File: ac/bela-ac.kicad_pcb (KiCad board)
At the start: 2 copper layers, 29 parts, among them P5 +/-15v, P6 15v_out, P7 belaaudioout, P8 belaaudioin, P9 mod_ac-io, U1 TL074

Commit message: consolidated schematics etc
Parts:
- removed R4: bead, xnorman:Resistor_Vertical_RM5mm-xnor
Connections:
- P6 pad 1: Net-(P6-Pad1) -> +15v

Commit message: removed ac from extra, added power connection for 15
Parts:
- P6: footprint Pin_Headers:Pin_Header_Straight_1x02_Pitch2.54mm -> mta-156:MTA-156-2
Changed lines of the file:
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@@
     )
   )
-  (module Pin_Headers:Pin_Header_Straight_1x02_Pitch2.54mm (layer F.Cu)
+  (module mta-156:MTA-156-2 (layer F.Cu)
     (at 95.7072 118.618 270)
-    (descr "Through hole straight pin header, 1x02, 2.54mm pitch, single row")
-    (tags "Through hole pin header THT 1x02 2.54mm single row")
-    (fp_text reference P6 (at 0 -2.39 270) (layer F.SilkS)
+    (descr MTA-156-2)
+    (tags MTA-156-2)
+    (fp_text reference P6 (at 0 -5.1 270) (layer F.SilkS)
       (effects (font (size 1 1) (thickness 0.15)))
     )
-    (fp_text value 15v_out (at 0 4.93 270) (layer F.Fab)
+    (fp_text value 15v_out (at 0 -3.1 270) (layer F.Fab)
       (effects (font (size 1 1) (thickness 0.15)))
     )
-    (fp_line (start -1.27 -1.27) (end -1.27 3.81) (layer F.Fab) (width 0.1))
-    (fp_line (start -1.27 3.81) (end 1.27 3.81) (layer F.Fab) (width 0.1))
-    (fp_line (start 1.27 3.81) (end 1.27 -1.27) (layer F.Fab) (width 0.1))
-    (fp_line (start 1.27 -1.27) (end -1.27 -1.27) (layer F.Fab) (width 0.1))
-    (fp_line (start -1.39 1.27) (end -1.39 3.93) (layer F.SilkS) (width 0.12))
-    (fp_line (start -1.39 3.93) (end 1.39 3.93) (layer F.SilkS) (width 0.12))
-    (fp_line (start 1.39 3.93) (end 1.39 1.27) (layer F.SilkS) (width 0.12))
-    (fp_line (start 1.39 1.27) (end -1.39 1.27) (layer F.SilkS) (width 0.12))
-    (fp_line (start -1.39 0) (end -1.39 -1.39) (layer F.SilkS) (width 0.12))
-    (fp_line (start -1.39 -1.39) (end 0 -1.39) (layer F.SilkS) (width 0.12))
-    (fp_line (start -1.6 -1.6) (end -1.6 4.1) (layer F.CrtYd) (width 0.05))
-    (fp_line (start -1.6 4.1) (end 1.6 4.1) (layer F.CrtYd) (width 0.05))
-    (fp_line (start 1.6 4.1) (end 1.6 -1.6) (layer F.CrtYd) (width 0.05))
-    (fp_line (start 1.6 -1.6) (end -1.6 -1.6) (layer F.CrtYd) (width 0.05))
-    (pad 1 thru_hole rect (at 0 0 270) (size 1.7 1.7) (drill 1) (layers *.Cu *.Mask)
+    (fp_line (start 3 -1.6) (end 3 5.6) (layer F.SilkS) (width 0.15))
+    (fp_line (start -4 -1.6) (end -4 5.6) (layer F.SilkS) (width 0.15))
+    (fp_line (start -2.6 -1.6) (end -2.6 5.6) (layer F.SilkS) (width 0.15))
+    (fp_line (start 3.2 -1.8) (end 3.2 5.8) (layer F.CrtYd) (width 0.15))
+    (fp_line (start -4.2 -1.8) (end -4.2 5.8) (layer F.CrtYd) (width 0.15))
+    (fp_line (start -4.2 -1.6) (end -2.6 -1.6) (layer F.SilkS) (width 0.15))
+    (fp_line (start -4.2 -1.6) (end 3 -1.6) (layer F.SilkS) (width 0.15))
+    (fp_line (start 3 5.6) (end -4 5.6) (layer F.SilkS) (width 0.15))
+    (fp_line (start 3.2 -1.8) (end -4.2 -1.8) (layer F.CrtYd) (width 0.15))
+    (fp_line (start -4.2 5.8) (end 3.2 5.8) (layer F.CrtYd) (width 0.15))
+    (pad 1 thru_hole oval (at 0 0 270) (size 5 2.5) (drill 1.68) (layers *.Cu *.Mask F.SilkS)
       (net 22 +15v))
-    (pad 2 thru_hole oval (at 0 2.54 270) (size 1.7 1.7) (drill 1) (layers *.Cu *.Mask)
+    (pad 2 thru_hole oval (at 0 3.96 270) (size 5 2.5) (drill 1.68) (layers *.Cu *.Mask F.SilkS)
       (net 1 GND))
-    (model Pin_Headers.3dshapes/Pin_Header_Straight_1x02_Pitch2.54mm.wrl
-      (at (xyz 0 -0.05 0))
-      (scale (xyz 1 1 1))
-      (rotate (xyz 0 0 90))
-    )
   )
   (gr_text "MOVE AC TO ANOTHER PCB AND PUT 15V in on this board?\n\nAdd mounting holes to AC board" (at 52.1716 109.1184) (layer F.SilkS)

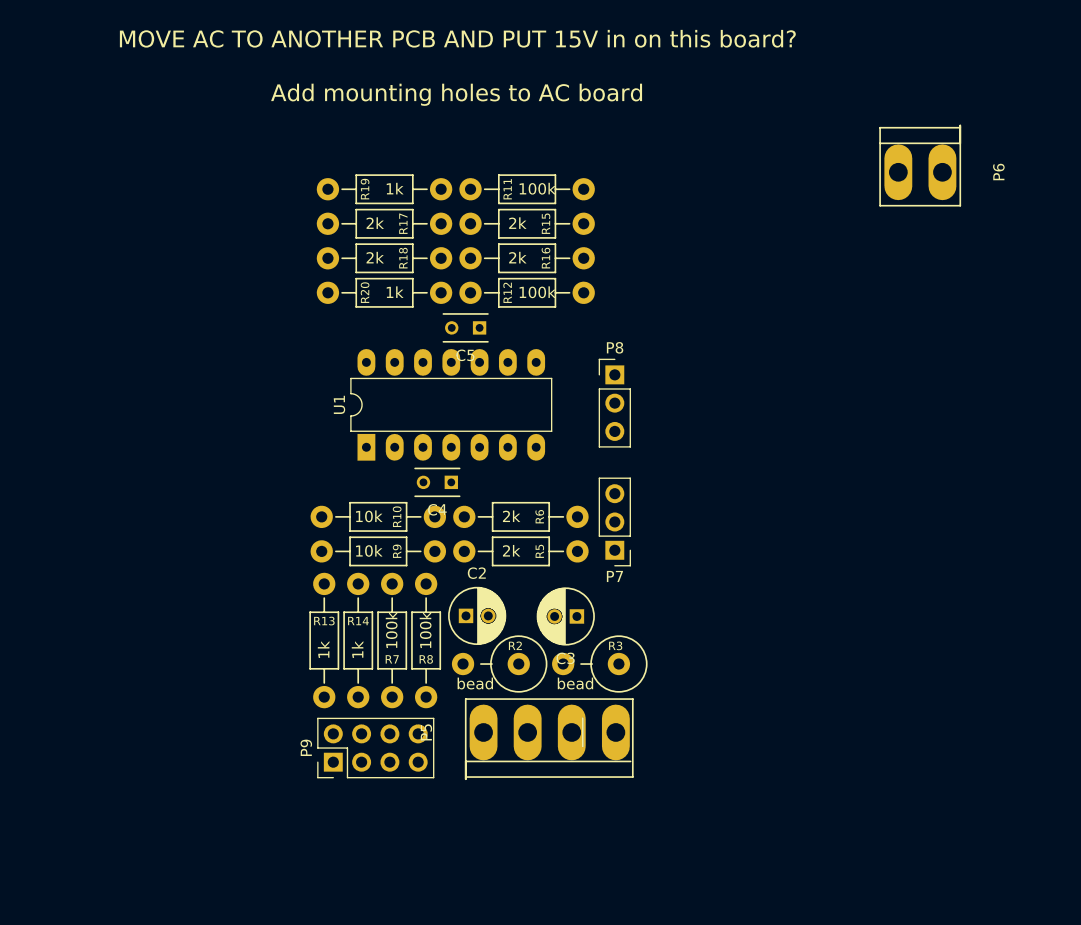
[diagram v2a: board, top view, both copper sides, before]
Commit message: added trimmer, removed b.s., almost ready to route
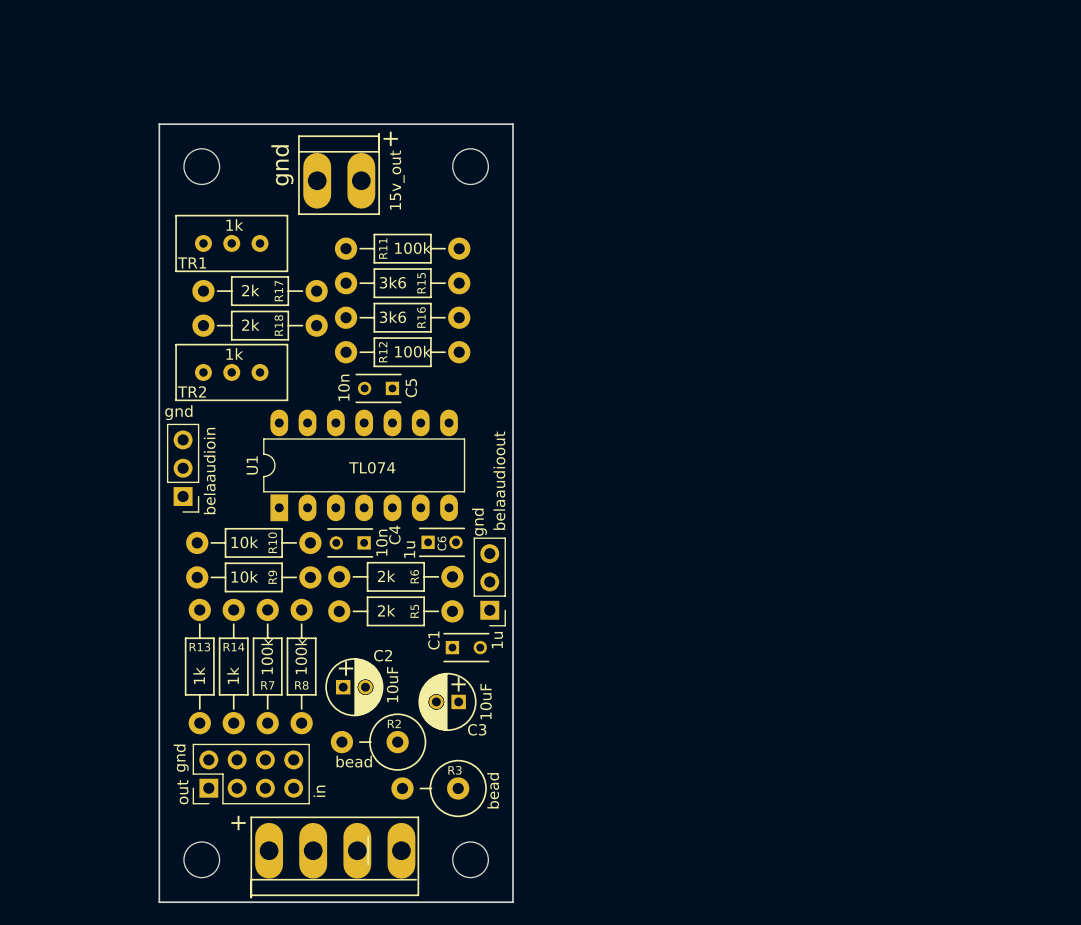
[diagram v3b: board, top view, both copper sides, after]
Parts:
- removed R19, R20: 1k, xnorman:Resistor_Horizontal_RM10mm-xnorman
- added C1: 1u, Capacitors_ThroughHole:C_Rect_L4_W2.5_P2.5, F.Cu at (51.7, 161.3)
- added C6: 1u, Capacitors_ThroughHole:C_Rect_L4_W2.5_P2.5, F.Cu at (49.5, 151.8)
- added REF1: MountingHole_3.2mm_M3, Mounting_Holes:MountingHole_3.2mm_M3, F.Cu at (29.2, 118.1)
- added REF2: MountingHole_3.2mm_M3, Mounting_Holes:MountingHole_3.2mm_M3, F.Cu at (53.3, 118.1)
- added REF3: MountingHole_3.2mm_M3, Mounting_Holes:MountingHole_3.2mm_M3, F.Cu at (53.3, 180.3)
- added REF4: MountingHole_3.2mm_M3, Mounting_Holes:MountingHole_3.2mm_M3, F.Cu at (29.2, 180.3)
- added TR1: 1k, trim:trimmer, F.Cu at (31.9, 127.5)
- added TR2: 1k, trim:trimmer, F.Cu at (31.9, 139.1)
- R15, R16: value 2k -> 3k6
- moved P6 52.2 mm to (43.5, 119.4)
- moved P8 40.3 mm to (27.5, 147.7), turned to 180 degrees
- moved P5 22.0 mm to (35.3, 179.5)
- moved R3 18.2 mm to (49.7, 173.9)
- moved C3 13.1 mm to (52.3, 166.2)
- moved R2 12.9 mm to (44.3, 169.8)
- moved C2 12.7 mm to (41.9, 164.8)
- moved R17 12.7 mm to (29.4, 129.3)
- moved R18 12.7 mm to (29.4, 132.4)
- moved R5 12.5 mm to (41.6, 158.0)
- moved P7 12.5 mm to (55.1, 157.9)
- moved R6 12.5 mm to (41.6, 154.9)
- moved R15 12.4 mm to (42.2, 128.6)
- moved R11 12.4 mm to (52.3, 125.5)
- moved R12 12.4 mm to (52.3, 134.8)
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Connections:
- R5 pad 2: belaacout1 -> Net-(C1-Pad1)
- R6 pad 2: belaacout2 -> Net-(C6-Pad1)
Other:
- board outline added: 31.8 x 69.9 mm
- board text added: "+"
- board text added: "gnd"
- board text added: "in"
- board text added: "out"
- board text removed: "MOVE AC TO ANOTHER PCB AND PUT 15V in on this board? Add mounting holes to AC board"

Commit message: totally routed, added labels
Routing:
- net +15v: track 0.00 -> 52.3 mm
- net -15v: track 0.00 -> 40.4 mm
- net Net-(R10-Pad1): track 0.00 -> 37.1 mm
- net Net-(R11-Pad2): track 0.00 -> 36.2 mm
- net Net-(R12-Pad2): track 0.00 -> 33.8 mm
- net belaacin1: track 0.00 -> 27.2 mm
- net Net-(R11-Pad1): track 0.00 -> 25.8 mm
- net belaacin2: track 0.00 -> 16.3 mm
- net Net-(R10-Pad2): track 0.00 -> 16.1 mm
- net Net-(P5-Pad1): track 0.00 -> 15.6 mm
- net Net-(R13-Pad2): track 0.00 -> 13.9 mm
- net Net-(R5-Pad1): track 0.00 -> 11.4 mm
- net Net-(R12-Pad1): track 0.00 -> 9.83 mm
- net Net-(R15-Pad1): track 0.00 -> 9.79 mm
- net Net-(R16-Pad1): track 0.00 -> 9.76 mm
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- added copper zone on B.Cu, net GND
- added copper zone on F.Cu, net GND
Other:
- board text added: "bela ac to modular"
- board text added: "http://x37v.info"
- board text added: "xnor 1/17"
